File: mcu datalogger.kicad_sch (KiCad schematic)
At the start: 25 parts, among them U1 24LC1025, U2 24LC1025, U3 DS1337S_, U4 ATMEGA328P-AU, Y1 Crystal, Y2 Crystal

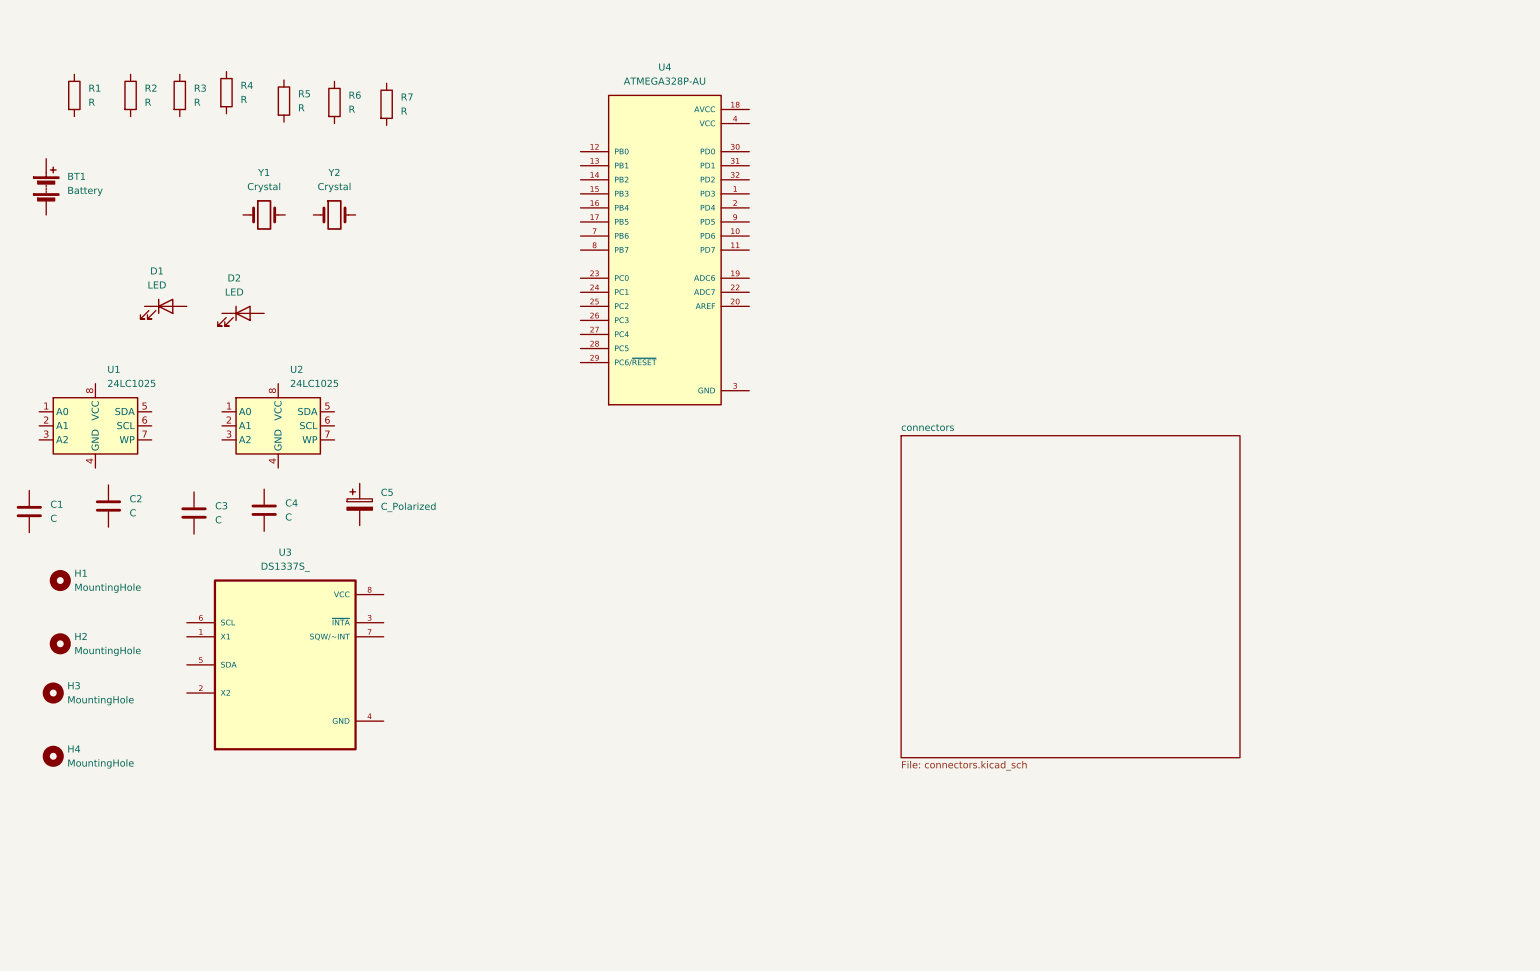
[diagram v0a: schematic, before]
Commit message: Update mcu datalogger.kicad_sch
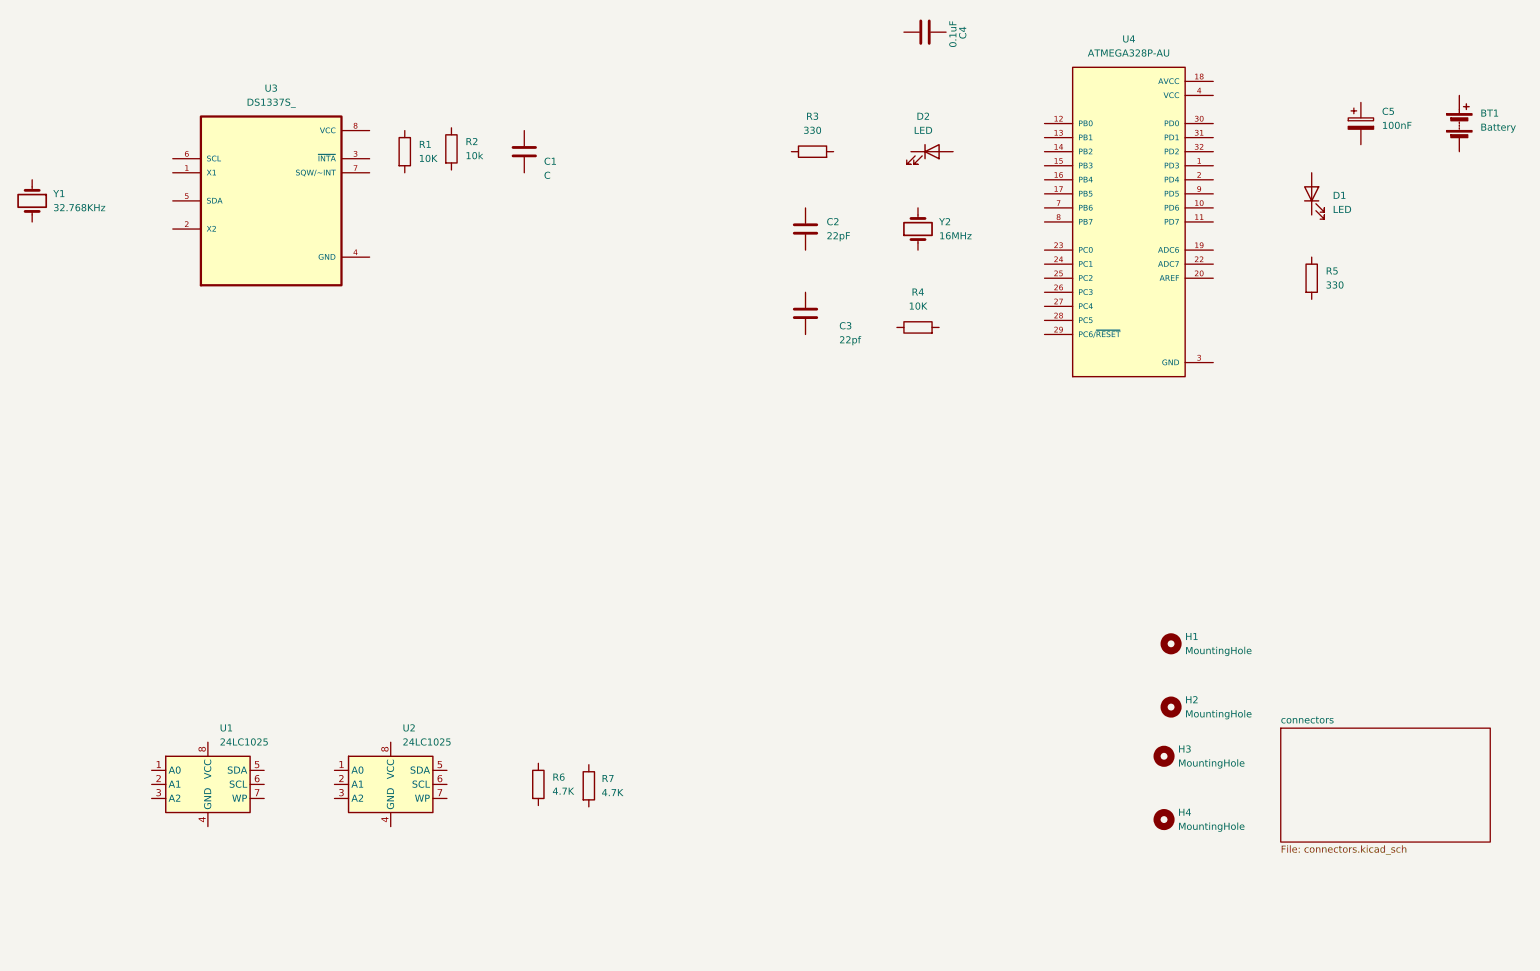
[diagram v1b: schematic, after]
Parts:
- C1: renamed from C4; footprint (none) -> 0.1uF
- C2: value C -> 22pF
- C3: value C -> 22pf
- C4: renamed from C1; value C -> 0.1uF
- C5: value C_Polarized -> 100nF
- R1: renamed from R3; value R -> 10K
- R2: renamed from R4; value R -> 10k
- R3: renamed from R2; value R -> 330
- R4: renamed from R7; value R -> 10K
- R5: renamed from R1; value R -> 330
- R6: renamed from R5; value R -> 4.7K
- R7: renamed from R6; value R -> 4.7K
- Y1: value Crystal -> 32.768KHz
- Y2: value Crystal -> 16MHz
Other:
- moved on the sheet: BT1, C1, C2, C3, C4, C5, D1, D2, H1, H2, H3, H4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

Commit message: Completed symbols to footprints associations
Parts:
- BT1: footprint (none) -> Connector_PinHeader_2.54mm:PinHeader_1x02_P2.54mm_Vertical
- C1: footprint 0.1uF -> Capacitor_SMD:C_0805_2012Metric
- C2, C3, C4, C5: footprint (none) -> Capacitor_SMD:C_0805_2012Metric
- D1, D2: footprint (none) -> LED_SMD:LED_0805_2012Metric
- H1, H2, H3, H4: footprint (none) -> MountingHole:MountingHole_2.1mm
- R1, R2, R3, R4, R5, R6, R7: footprint (none) -> Resistor_SMD:R_0805_2012Metric
- U1, U2: footprint (none) -> Package_SO:SOIC-8_5.3x5.3mm_P1.27mm
- U3: footprint DS1337S_:SOIC127P600X175-8N -> footprints:SOIC127P600X175-8N
- U4: footprint ATMEGA328P-AU:QFP80P900X900X120-32N -> footprints:QFP80P900X900X120-32N (2)
- Y1, Y2: footprint (none) -> Crystal:Crystal_SMD_5032-2Pin_5.0x3.2mm_HandSoldering
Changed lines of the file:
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@@
 			)
 		)
-		(property "Footprint" ""
+		(property "Footprint" "MountingHole:MountingHole_2.1mm"
 			(at 223.52 127 0)
 			(effects
@@
 			)
 		)
-		(property "Footprint" ""
+		(property "Footprint" "MountingHole:MountingHole_2.1mm"
 			(at 222.25 158.75 0)
 			(effects
@@
 			)
 		)
-		(property "Footprint" ""
+		(property "Footprint" "Capacitor_SMD:C_0805_2012Metric"
 			(at 182.88 15.5448 0)
 			(effects
@@
 			)
 		)
-		(property "Footprint" "0.1uF"
+		(property "Footprint" "Capacitor_SMD:C_0805_2012Metric"
 			(at 107.6452 41.91 0)
 			(effects
@@
 			)
 		)
-		(property "Footprint" ""
+		(property "Footprint" "Crystal:Crystal_SMD_5032-2Pin_5.0x3.2mm_HandSoldering"
 			(at 177.8 52.07 0)
 			(effects
@@
 			)
 		)
-		(property "Footprint" ""
+		(property "Footprint" "Capacitor_SMD:C_0805_2012Metric"
 			(at 258.7752 36.83 0)
 			(effects
@@
 			)
 		)
-		(property "Footprint" ""
+		(property "Footprint" "Resistor_SMD:R_0805_2012Metric"
 			(at 107.442 152.4 90)
 			(effects
@@
 			)
 		)
-		(property "Footprint" ""
+		(property "Footprint" "MountingHole:MountingHole_2.1mm"
 			(at 222.25 147.32 0)
 			(effects
@@
 			)
 		)
-		(property "Footprint" ""
+		(property "Footprint" "MountingHole:MountingHole_2.1mm"
 			(at 223.52 138.43 0)
 			(effects
@@
 			)
 		)
-		(property "Footprint" ""
+		(property "Footprint" "Resistor_SMD:R_0805_2012Metric"
 			(at 91.7423 37.5963 90)
 			(effects
@@
 			)
 		)
-		(property "Footprint" ""
+		(property "Footprint" "Resistor_SMD:R_0805_2012Metric"
 			(at 158.75 39.878 90)
 			(effects
@@
 			)
 		)
-		(property "Footprint" ""
+		(property "Footprint" "Package_SO:SOIC-8_5.3x5.3mm_P1.27mm"
 			(at 49.53 152.4 0)
 			(effects
@@
 			)
 		)
-		(property "Footprint" ""
+		(property "Footprint" "Connector_PinHeader_2.54mm:PinHeader_1x02_P2.54mm_Vertical"
 			(at 275.59 31.496 90)
 			(effects
@@
 			)
 		)
-		(property "Footprint" ""
+		(property "Footprint" "Capacitor_SMD:C_0805_2012Metric"
 			(at 158.4452 71.12 0)
 			(effects
@@
 			)
 		)
-		(property "Footprint" "DS1337S_:SOIC127P600X175-8N"
+		(property "Footprint" "footprints:SOIC127P600X175-8N"
 			(at 60.96 46.99 0)
 			(effects
@@
 			)
 		)
-		(property "Footprint" ""
+		(property "Footprint" "Crystal:Crystal_SMD_5032-2Pin_5.0x3.2mm_HandSoldering"
 			(at 17.78 46.99 0)
 			(effects
@@
 			)
 		)
-		(property "Footprint" ""
+		(property "Footprint" "Package_SO:SOIC-8_5.3x5.3mm_P1.27mm"
 			(at 82.55 152.4 0)
 			(effects
@@
 			)
 		)
-		(property "Footprint" "ATMEGA328P-AU:QFP80P900X900X120-32N"
+		(property "Footprint" "footprints:QFP80P900X900X120-32N (2)"
 			(at 215.9 50.8 0)
 			(effects
@@
 			)
 		)
-		(property "Footprint" ""
+		(property "Footprint" "Resistor_SMD:R_0805_2012Metric"
 			(at 247.142 60.96 90)
 			(effects
@@
 			)
 		)
-		(property "Footprint" ""
+		(property "Footprint" "Resistor_SMD:R_0805_2012Metric"
 			(at 116.5635 152.6534 90)
 			(effects
@@
 			)
 		)
-		(property "Footprint" ""
+		(property "Footprint" "Resistor_SMD:R_0805_2012Metric"
 			(at 177.8 71.628 90)
 			(effects
@@
 			)
 		)
-		(property "Footprint" ""
+		(property "Footprint" "Capacitor_SMD:C_0805_2012Metric"
 			(at 158.4452 55.88 0)
 			(effects
@@
 			)
 		)
-		(property "Footprint" ""
+		(property "Footprint" "LED_SMD:LED_0805_2012Metric"
 			(at 248.92 45.72 0)
 			(effects
@@
 			)
 		)
-		(property "Footprint" ""
+		(property "Footprint" "Resistor_SMD:R_0805_2012Metric"
 			(at 83.312 38.1 90)
 			(effects
@@
 			)
 		)
-		(property "Footprint" ""
+		(property "Footprint" "LED_SMD:LED_0805_2012Metric"
 			(at 180.34 38.1 0)
 			(effects

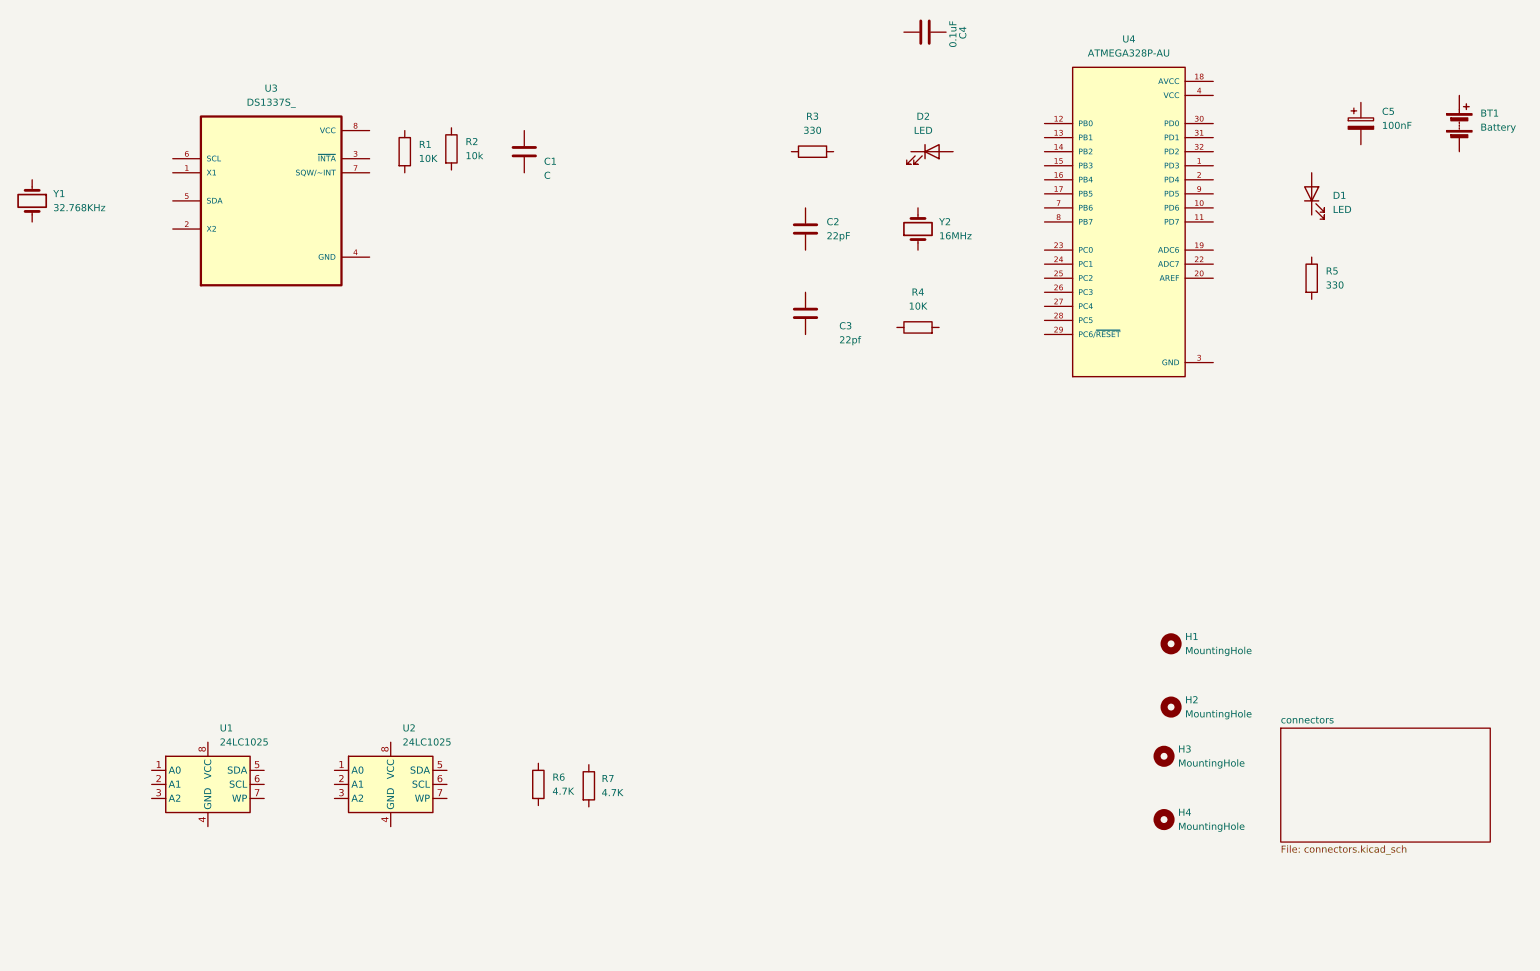
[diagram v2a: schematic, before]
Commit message: Completed wiring of main sheet
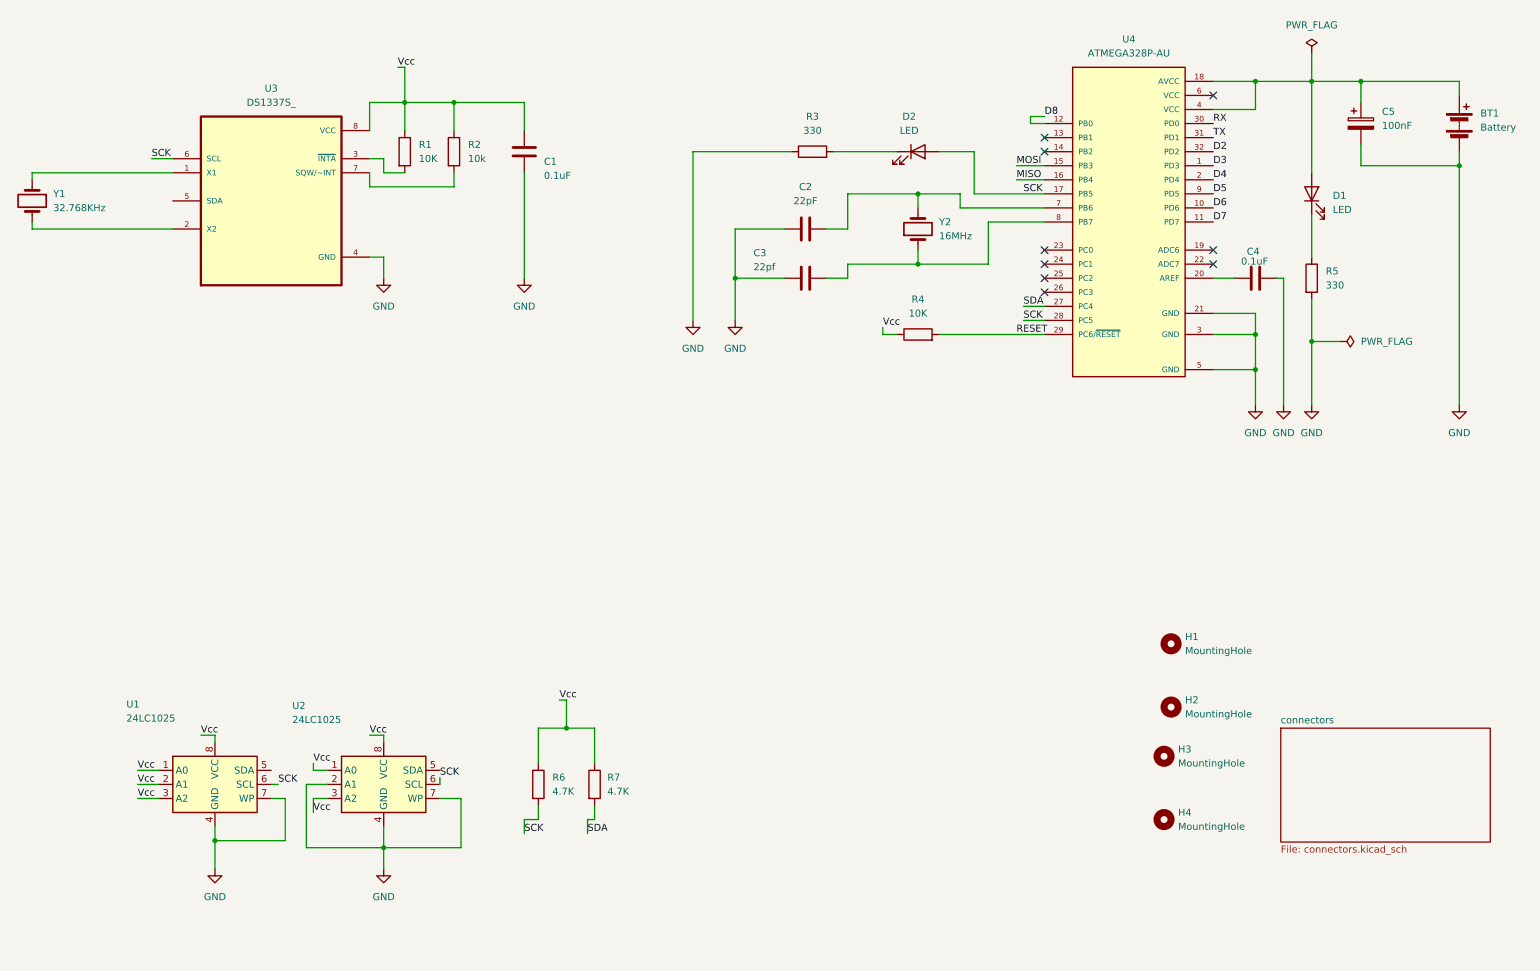
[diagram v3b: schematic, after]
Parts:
- C1: value C -> 0.1uF
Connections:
- net GND: now also BT1.2 (-), C1.2, C2.1, C3.1, C4.2, C5.2, R3.1, R5.2, U1.4 (GND), U1.7 (WP), U2.2 (A1), U2.4 (GND), U2.7 (WP), U3.4 (GND)
- net at C4.1: now also U4.20 (AREF)
- net Vcc: now reaches C1.1
- net Vcc: now also R1.1, R2.1, R4.1, R6.1, R7.1, U1.1 (A0), U1.2 (A1), U1.3 (A2), U1.8 (VCC), U2.1 (A0), U2.3 (A2), U2.8 (VCC), U3.8 (VCC)
- net at Y2.1: now also C3.2, U4.8 (PB7)
- net at Y2.2: now also C2.2, U4.7 (PB6)
- net at C5.1: now also BT1.1 (+), D1.2 (A), U4.18 (AVCC), U4.4 (VCC)
- net SCK: now reaches R6.2
- net SCK: now also D2.2 (A), U1.6 (SCL), U2.6 (SCL), U3.6 (SCL), U4.17 (PB5), U4.28 (PC5)
- net at R2.2: now also U3.7 (SQW/~INT)
- net at R3.2: now also D2.1 (K)
- net at U3.1 (X1): now also Y1.1
- net at U3.2 (X2): now also Y1.2
- net at U3.3 (~{INTA}): now also R1.2
- net D3: now reaches U4.1 (PD3)
- net D6: now reaches U4.10 (PD6)
- net D7: now reaches U4.11 (PD7)
- net D8: now reaches U4.12 (PB0)
- net MOSI: now reaches U4.15 (PB3)
- net MISO: now reaches U4.16 (PB4)
- net D4: now reaches U4.2 (PD4)
- net SDA: now reaches U4.27 (PC4)
- net SDA: now also R7.2
- net RESET: now reaches U4.29 (PC6/~{RESET})
- net RESET: now also R4.2
- net RX: now reaches U4.30 (PD0)
- net TX: now reaches U4.31 (PD1)
- net D2: now reaches U4.32 (PD2)
- net D5: now reaches U4.9 (PD5)
- net at R5.1: now also D1.1 (K)
- net VCC: no longer names the net of U4.6 (VCC)
- net VCC: no longer U4.4 (VCC)
- no-connect marks 0 -> 9
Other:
- moved on the sheet: C2, C3, C4, D2, R2, R4, R7, U1, U2

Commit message: Completed wiring and ERC check for root sheet
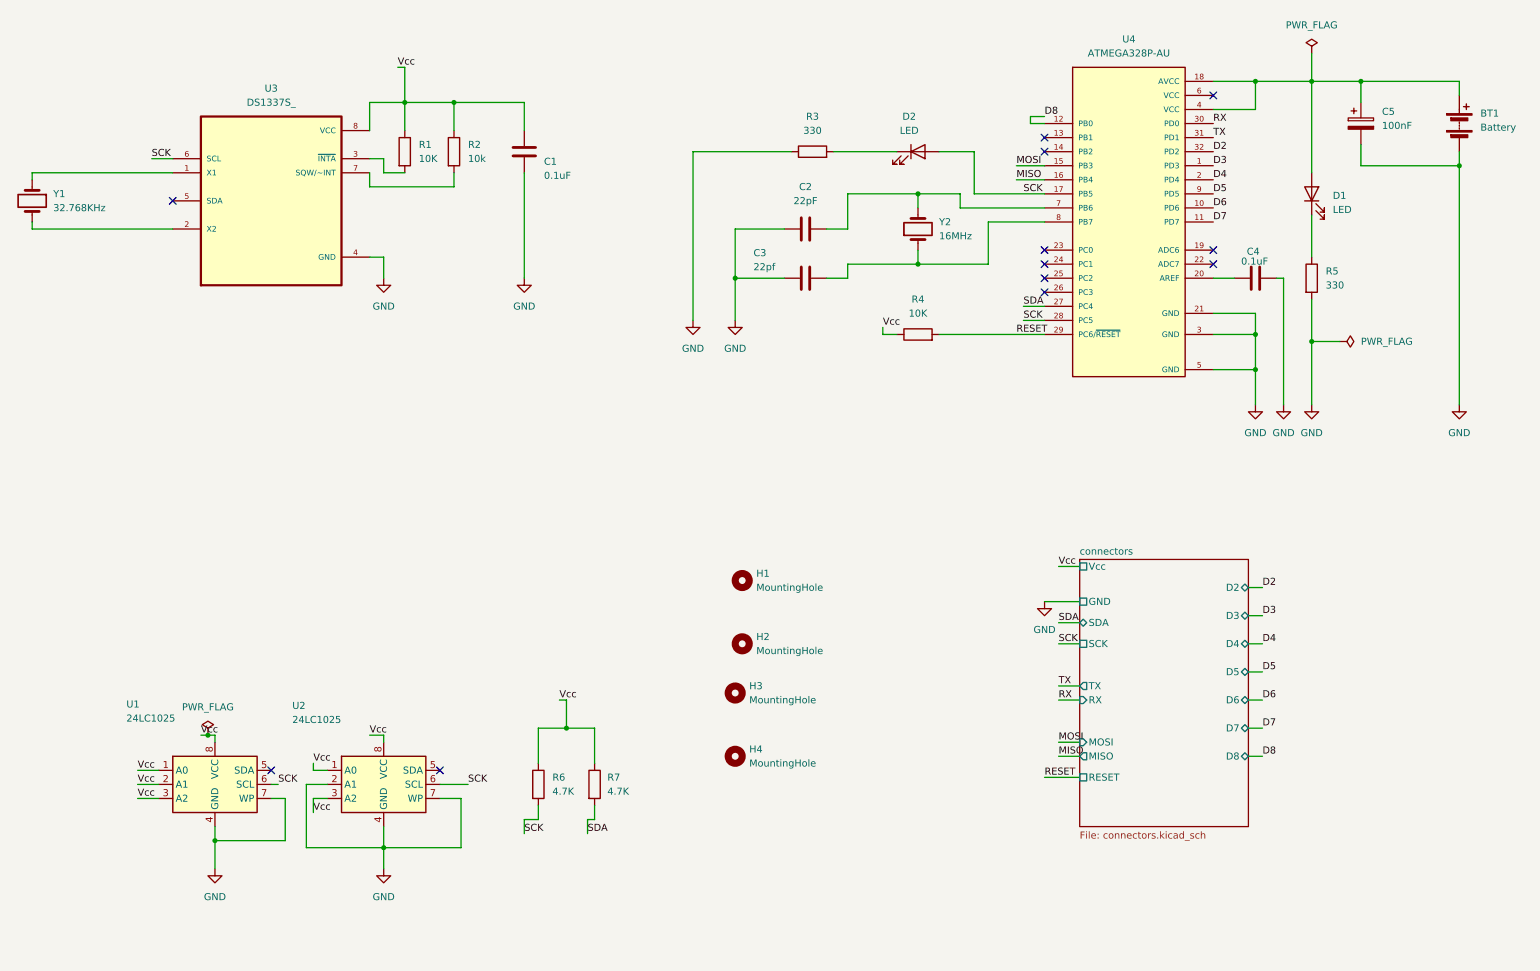
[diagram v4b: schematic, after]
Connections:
- no-connect marks 9 -> 12
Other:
- sheet connectors ports: added D2, D3, D4, D5, D6, D7, D8, GND, MISO, MOSI, RESET, RX, SCK, SDA, TX, Vcc; removed none
- moved on the sheet: H1, H2, H3, H4

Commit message: Completed comments
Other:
- note added: "EEPROM"
- note added: "MCU"
- note added: "Mounting hole"
- note added: "Real time clock"
- moved on the sheet: BT1, C2, C3, C4, C5, D1, D2, R3, R4, R5, R6, R7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
